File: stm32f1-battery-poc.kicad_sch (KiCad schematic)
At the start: 138 parts, among them J1 Conn_01x02, J10 Conn_02x02_Odd_Even, J11 Conn_02x02_Odd_Even, J12 Conn_01x04_Pin, J2 Conn_02x07_Odd_Even, J3 Conn_01x02, J7 Conn_02x02_Odd_Even, J8 Conn_02x03_Odd_Even, J9 Conn_02x03_Odd_Even, M1 Motor_3_Phases, M2 Stepper_Motor_bipolar, Q1 Q_NMOS, Q2 Q_NMOS, SW1 SW_Push, SW2 SW_Push, SW3 SW_SPST, SW4 SW_Push, U1 LM78M05, U10 DRV8424RGER, U2 HT753-1, U3 SN65HVD230, U4 DRV8311H, U5 STM32F103C8Tx, U6 QRE1113GR, U7 QRE1113GR, U8 QRE1113GR, U9 BQ77905, Y1 8M

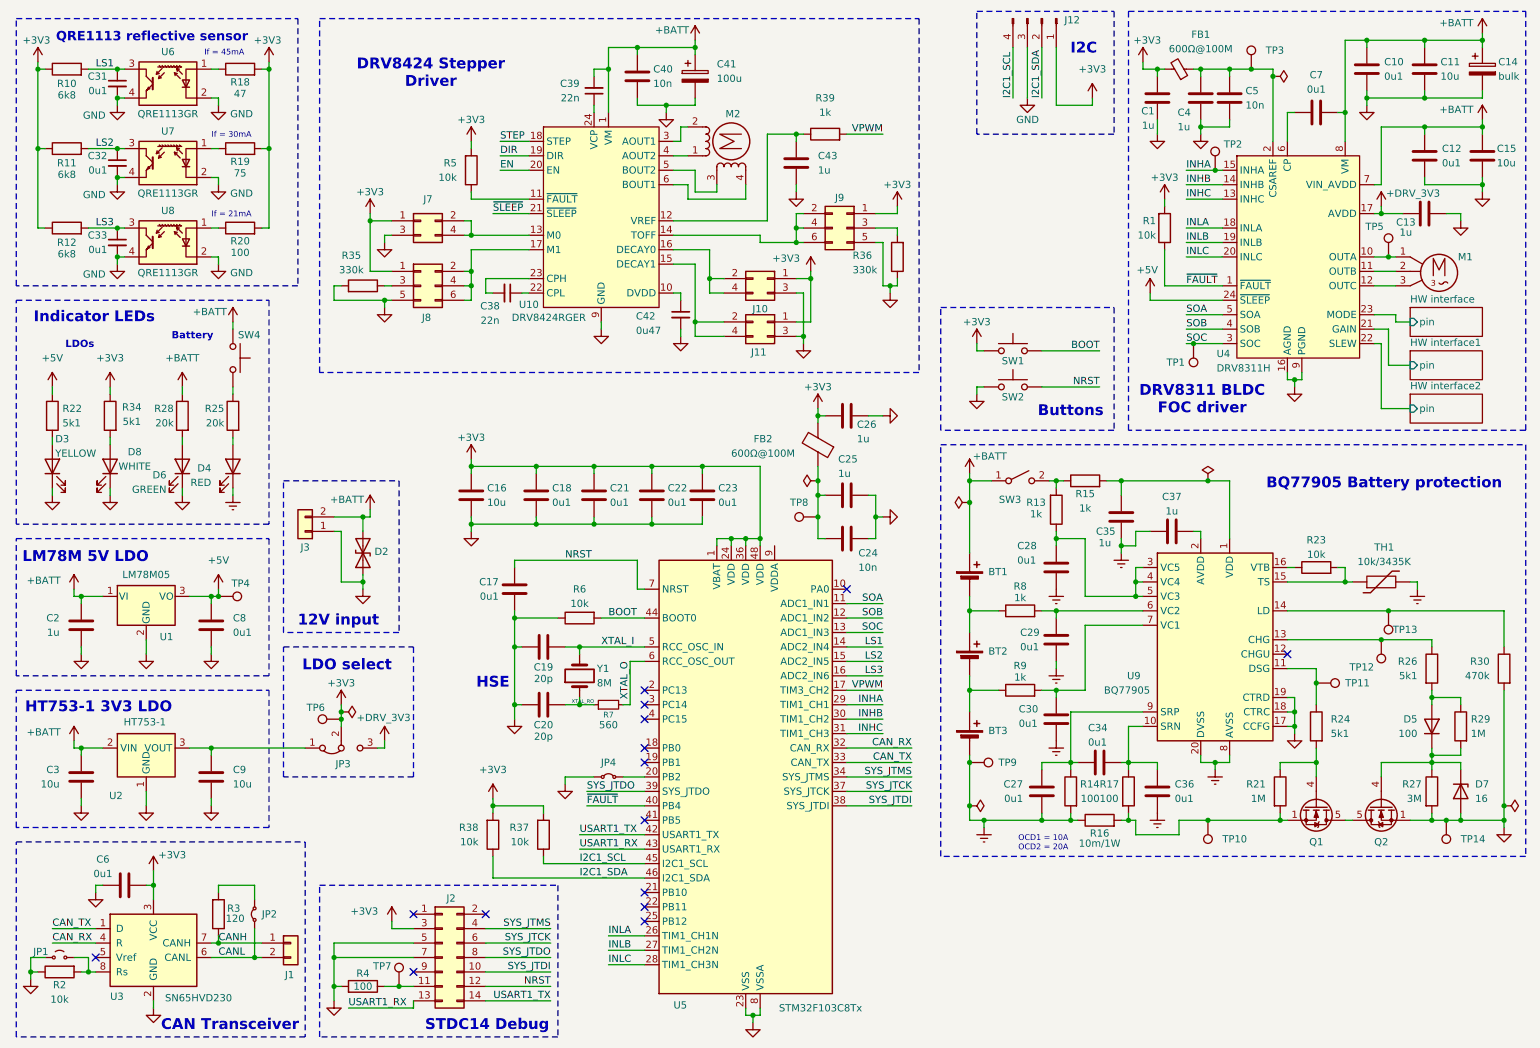
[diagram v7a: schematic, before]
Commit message: schem: add footprints and ordering info to BOM
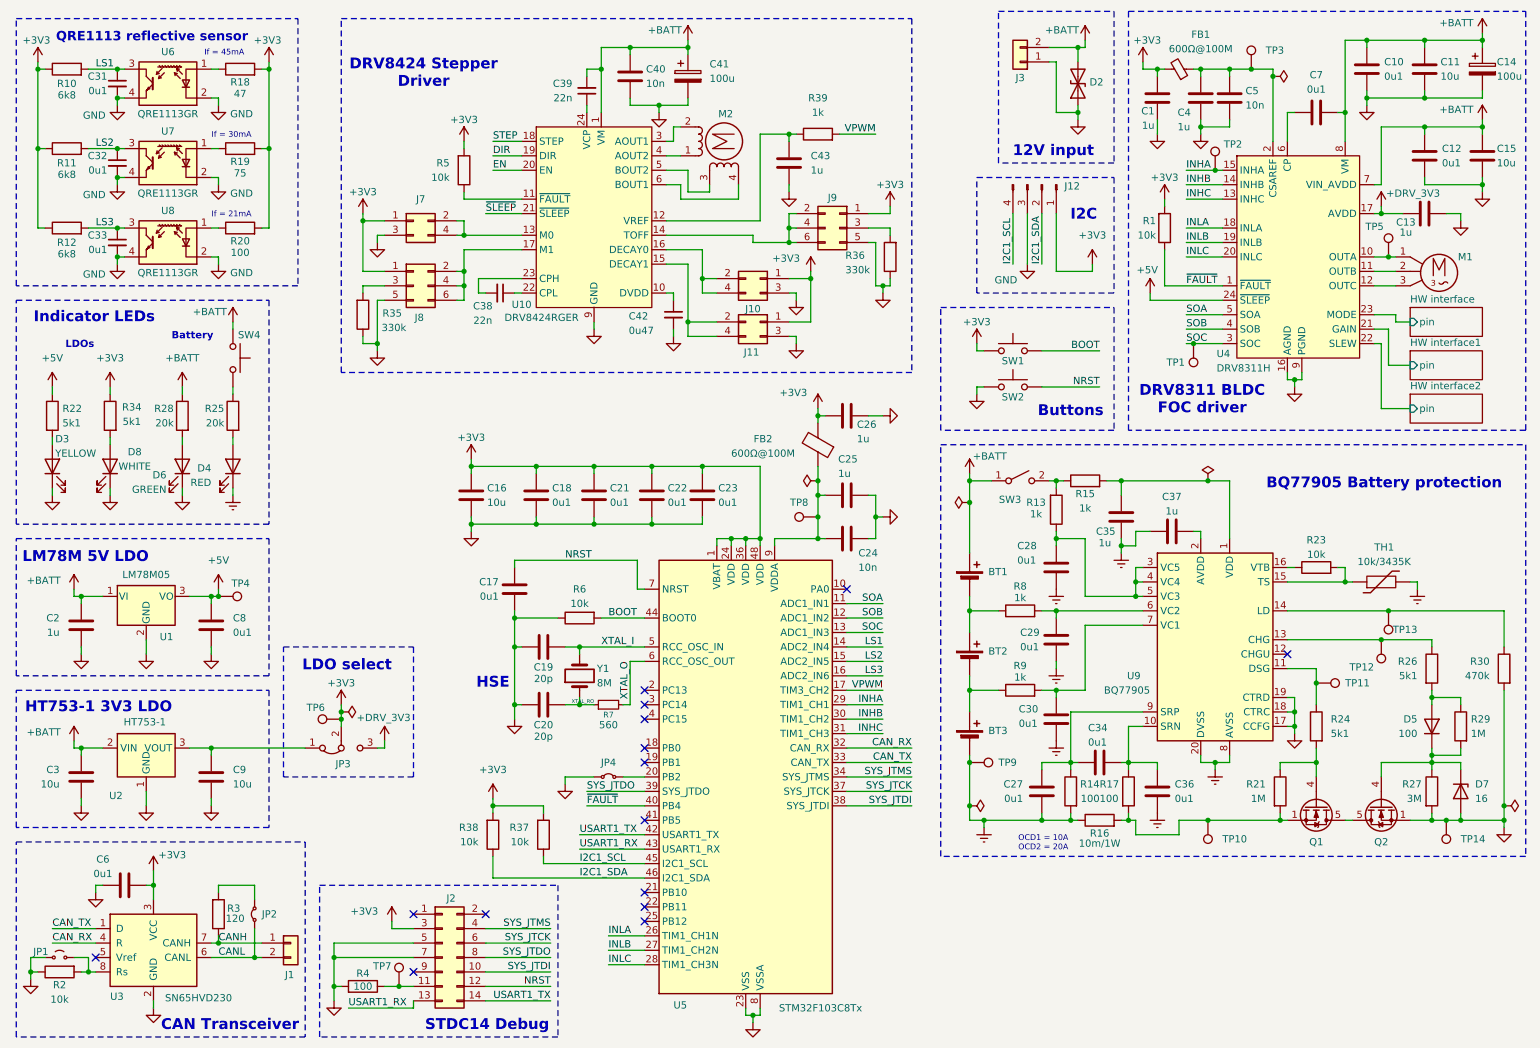
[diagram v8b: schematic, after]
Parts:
- BT1, BT2, BT3: footprint (none) -> GLCS:BatteryHolder_MYOUNG_BH-18650-B1BA002; now left out of the parts list
- C1, C13, C2, C25, C26, C35, C37, C4, C43: footprint (none) -> Capacitor_SMD:C_0402_1005Metric; Basic (none) -> Y; JLCPCB Part # (none) -> C52923; Manufacturer (none) -> Samsung Electro-Mechanics; Manufacturer Part Number (none) -> CL05A105KA5NQNC
- C10, C12, C17, C18, C21, C22, C23, C27, C28, C29, C30, C34, C36, C6, C7, C8: footprint (none) -> Capacitor_SMD:C_0402_1005Metric; Basic (none) -> Y; JLCPCB Part # (none) -> C307331; Manufacturer (none) -> Samsung Electro-Mechanics; Manufacturer Part Number (none) -> CL05B104KB54PNC
- C11, C15, C16, C3, C9: footprint (none) -> Capacitor_SMD:C_0805_2012Metric; Basic (none) -> Y; JLCPCB Part # (none) -> C440198; Manufacturer (none) -> Murata; Manufacturer Part Number (none) -> GRM21BR61H106KE43L
- C14: value bulk -> 100u; footprint (none) -> Capacitor_SMD:CP_Elec_6.3x7.7; Basic (none) -> X; JLCPCB Part # (none) -> C165974; Manufacturer (none) -> PANASONIC; Manufacturer Part Number (none) -> EEEFTH101XAP
- C19, C20: JLCPCB Part # 0603CG300J500NT -> C1658
- C24, C40, C5: footprint (none) -> Capacitor_SMD:C_0402_1005Metric; Basic (none) -> Y; JLCPCB Part # (none) -> C15195; Manufacturer (none) -> Samsung Electro-Mechanics; Manufacturer Part Number (none) -> CL05B103KB5NNNC
- C38, C39: footprint (none) -> Capacitor_SMD:C_0402_1005Metric; Basic (none) -> Y; JLCPCB Part # (none) -> C1532; Manufacturer (none) -> FH (Guangdong Fenghua Advanced Tech); Manufacturer Part Number (none) -> 0402B223K500NT
- C41: footprint (none) -> Capacitor_SMD:CP_Elec_6.3x7.7; Basic (none) -> X; JLCPCB Part # (none) -> C165974; Manufacturer (none) -> PANASONIC; Manufacturer Part Number (none) -> EEEFTH101XAP
- C42: footprint (none) -> Capacitor_SMD:C_0603_1608Metric; Basic (none) -> Y; JLCPCB Part # (none) -> C1623; Manufacturer (none) -> Samsung Electro-Mechanics; Manufacturer Part Number (none) -> CL10B474KA8NNNC
- FB1, FB2: footprint (none) -> Inductor_SMD:L_0805_2012Metric; Basic (none) -> Y; JLCPCB Part # (none) -> C1015; Manufacturer (none) -> Sunlord; Manufacturer Part Number (none) -> GZ2012D101TF
- J1, SW3: footprint (none) -> Connector_PinHeader_2.54mm:PinHeader_1x02_P2.54mm_Vertical; now left out of the parts list
- J10, J11, J7: footprint (none) -> Connector_PinHeader_1.27mm:PinHeader_2x02_P1.27mm_Vertical; now left out of the parts list
- J2: footprint (none) -> Connector_PinHeader_1.27mm:PinHeader_2x07_P1.27mm_Vertical; now left out of the parts list
- J8, J9: footprint (none) -> Connector_PinHeader_1.27mm:PinHeader_2x03_P1.27mm_Vertical; now left out of the parts list
- JP1, JP2, JP4: footprint (none) -> Connector_PinHeader_1.27mm:PinHeader_2x01_P1.27mm_Vertical; now left out of the parts list
- M1: footprint (none) -> Connector_PinHeader_2.54mm:PinHeader_1x03_P2.54mm_Vertical; now left out of the parts list
- M2: footprint (none) -> GLCS:JST_XH_S6B-XH-A_Stepper_1x06_P2.50mm_Horizontal; now left out of the parts list
- R1, R2, R23, R37, R38, R5, R6: footprint (none) -> Resistor_SMD:R_0402_1005Metric; Basic (none) -> Y; JLCPCB Part # (none) -> C25744; Manufacturer (none) -> Uniroyal Elec; Manufacturer Part Number (none) -> 0402WGF1002TCE
- R13, R15, R39, R8, R9: footprint (none) -> Resistor_SMD:R_0402_1005Metric; Basic (none) -> Y; JLCPCB Part # (none) -> C11702; Manufacturer (none) -> Uniroyal Elec; Manufacturer Part Number (none) -> 0402WGF1001TCE
- R14, R17, R4: footprint (none) -> Resistor_SMD:R_0402_1005Metric; Basic (none) -> Y; JLCPCB Part # (none) -> C25076; Manufacturer (none) -> Uniroyal Elec; Manufacturer Part Number (none) -> 0402WGF1000TCE
- R16: footprint (none) -> Resistor_SMD:R_1206_3216Metric; Basic (none) -> X; JLCPCB Part # (none) -> C105362; Manufacturer (none) -> PSA(Prosperity Dielectrics); Manufacturer Part Number (none) -> FMF06FTHR010-LH
- R21, R29: footprint (none) -> Resistor_SMD:R_0402_1005Metric; Basic (none) -> Y; JLCPCB Part # (none) -> C26083; Manufacturer (none) -> Uniroyal Elec; Manufacturer Part Number (none) -> 0402WGF1004TCE
- R25, R28: footprint (none) -> Resistor_SMD:R_0603_1608Metric; Basic (none) -> Y; JLCPCB Part # (none) -> C4184; Manufacturer (none) -> Uniroyal Elec; Manufacturer Part Number (none) -> 0603WAF2002T5E
- R27: footprint (none) -> Resistor_SMD:R_0603_1608Metric; Basic (none) -> E; JLCPCB Part # (none) -> C23156; Manufacturer (none) -> Uniroyal Elec; Manufacturer Part Number (none) -> 0603WAF3004T5E
- R3: footprint (none) -> Resistor_SMD:R_1206_3216Metric; Basic (none) -> Y; JLCPCB Part # (none) -> C17909; Manufacturer (none) -> Uniroyal Elec; Manufacturer Part Number (none) -> 1206W4F1200T5E
- R30: footprint (none) -> Resistor_SMD:R_0603_1608Metric; Basic (none) -> Y; JLCPCB Part # (none) -> C23178; Manufacturer (none) -> Uniroyal Elec; Manufacturer Part Number (none) -> 0603WAF4703T5E
- R35, R36: footprint (none) -> Resistor_SMD:R_0603_1608Metric; Basic (none) -> Y; JLCPCB Part # (none) -> C23137; Manufacturer (none) -> Uniroyal Elec; Manufacturer Part Number (none) -> 0603WAF3303T5E
- TH1: footprint (none) -> Connector_PinSocket_2.54mm:PinSocket_1x02_P2.54mm_Vertical; now left out of the parts list
- TP1, TP10, TP11, TP12, TP13, TP14, TP2, TP3, TP4, TP5, TP6, TP7, TP8, TP9: footprint (none) -> TestPoint:TestPoint_Pad_D2.0mm; now left out of the parts list
- U1: Basic (none) -> X; JLCPCB Part # (none) -> C5145267; Manufacturer (none) -> HANSCHIP semiconductor; Manufacturer Part Number (none) -> LM78M05ACKTPRG
- U10: Basic (none) -> X; JLCPCB Part # (none) -> C1518725; Manufacturer (none) -> Texas Instruments; Manufacturer Part Number (none) -> DRV8424RGER
- U2: Basic (none) -> Y; JLCPCB Part # (none) -> C14289; Manufacturer (none) -> Holtek Semicon; Manufacturer Part Number (none) -> HT7533-1
- U3: Basic (none) -> E; JLCPCB Part # (none) -> C12084; Manufacturer (none) -> Texas Instruments; Manufacturer Part Number (none) -> SN65HVD230DR
- U4: footprint (none) -> GLCS:Texas_RRW0024A_WQFN-24-1EP_2x2mm_P0.4mmThermalVias; Basic (none) -> X; JLCPCB Part # (none) -> C5218862; Manufacturer (none) -> Texas Instruments; Manufacturer Part Number (none) -> DRV8311HRRWR
- U5: Basic (none) -> E; JLCPCB Part # (none) -> C8734; Manufacturer (none) -> STMicroelectronics; Manufacturer Part Number (none) -> STM32F103C8T6
- U9: Basic (none) -> X; JLCPCB Part # (none) -> C2866527; Manufacturer (none) -> Texas Instruments; Manufacturer Part Number (none) -> BQ7790509PWR
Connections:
- net EPAD: now also R35.1; no longer R35.2
- net at J8.3 (Pin_3): now also R35.2; no longer R35.1
- net at U5.9 (VDDA): now also C24.1, C25.1, FB2.1, TP8.1
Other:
- moved on the sheet: C38, C39, C40, C41, C42, C43, D2, J10, J11, J12, J3, J7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
